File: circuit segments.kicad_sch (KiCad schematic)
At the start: 0 parts

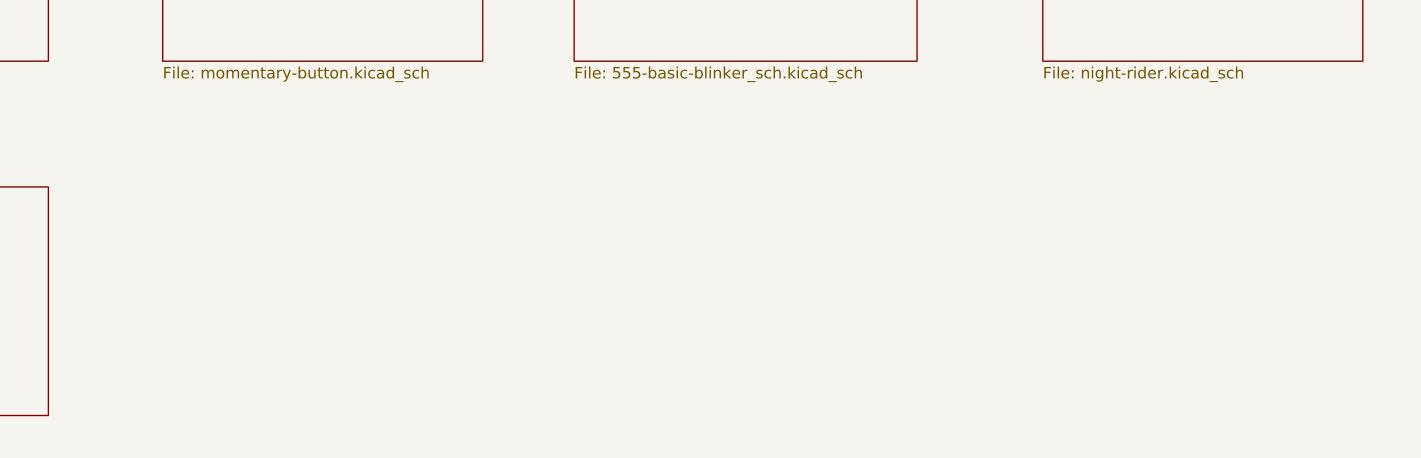
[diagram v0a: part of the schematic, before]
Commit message: new pages added
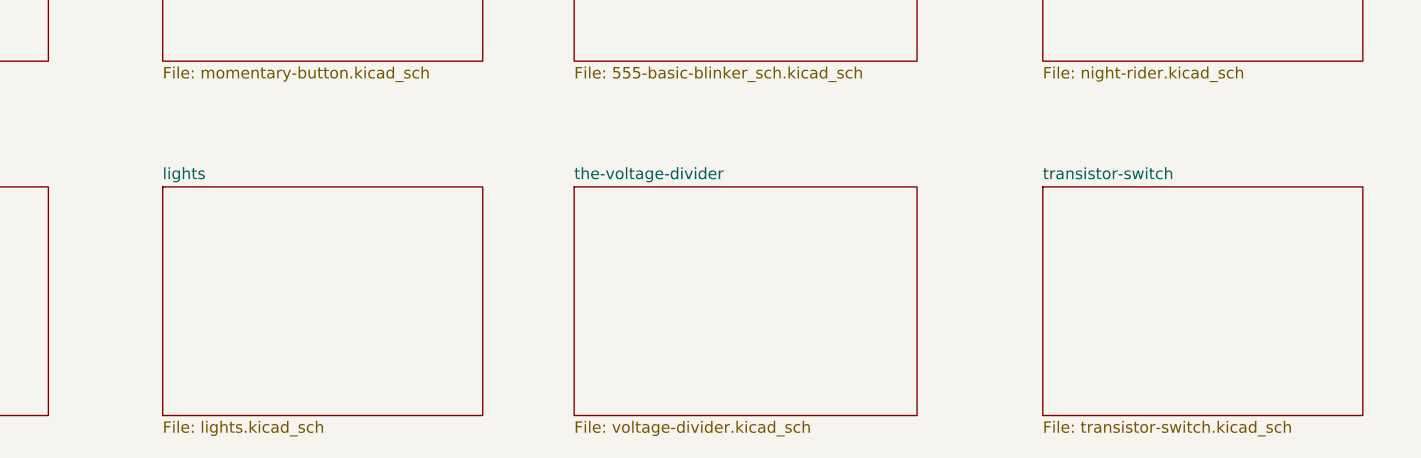
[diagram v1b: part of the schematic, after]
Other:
- added sheet lights (lights.kicad_sch)
- added sheet the-voltage-divider (voltage-divider.kicad_sch)
- added sheet transistor-switch (transistor-switch.kicad_sch)
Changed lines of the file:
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@@
+	)
+	(sheet
+		(at 184.15 92.71)
+		(size 35.56 25.4)
+		(fields_autoplaced yes)
+		(stroke
+			(width 0.1524)
+			(type solid)
+		)
+		(fill
+			(color 0 0 0 0.0000)
+		)
+		(property "Sheetname" "transistor-switch"
+			(at 184.15 91.9984 0)
+			(effects
+				(font
+					(size 1.27 1.27)
+				)
+				(justify left bottom)
+			)
+		)
+		(property "Sheetfile" "transistor-switch.kicad_sch"
+			(at 184.15 118.6946 0)
+			(effects
+				(font
+					(size 1.27 1.27)
+				)
+				(justify left top)
+			)
+		)
+		(instances
+			(project "circuit segments"
+				(path "/6128aede-be38-412f-a65d-6dbf7377b853"
+					(page "9")
+				)
+			)
+		)
 	)
 	(sheet
@@
 				)
 			)
+		)
+	)
+	(sheet
+		(at 86.36 92.71)
+		(size 35.56 25.4)
+		(fields_autoplaced yes)
+		(stroke
+			(width 0.1524)
+			(type solid)
+		)
+		(fill
+			(color 0 0 0 0.0000)
+		)
+		(property "Sheetname" "lights"
+			(at 86.36 91.9984 0)
+			(effects
+				(font
+					(size 1.27 1.27)
+				)
+				(justify left bottom)
+			)
+		)
+		(property "Sheetfile" "lights.kicad_sch"
+			(at 86.36 118.6946 0)
+			(effects
+				(font
+					(size 1.27 1.27)
+				)
+				(justify left top)
+			)
+		)
+		(instances
+			(project "circuit segments"
+				(path "/6128aede-be38-412f-a65d-6dbf7377b853"
+					(page "7")
+				)
+			)
+		)
+	)
+	(sheet
+		(at 132.08 92.71)
+		(size 38.1 25.4)
+		(fields_autoplaced yes)
+		(stroke
+			(width 0.1524)
+			(type solid)
+		)
+		(fill
+			(color 0 0 0 0.0000)
+		)
+		(property "Sheetname" "the-voltage-divider"
+			(at 132.08 91.9984 0)
+			(effects
+				(font
+					(size 1.27 1.27)
+				)
+				(justify left bottom)
+			)
+		)
+		(property "Sheetfile" "voltage-divider.kicad_sch"
+			(at 132.08 118.6946 0)
+			(effects
+				(font
+					(size 1.27 1.27)
+				)
+				(justify left top)
+			)
+		)
+		(property "Field2" ""
+			(at 132.08 92.71 0)
+			(effects
+				(font
+					(size 1.27 1.27)
+				)
+				(hide yes)
+			)
+		)
+		(instances
+			(project "circuit segments"
+				(path "/6128aede-be38-412f-a65d-6dbf7377b853"
+					(page "8")
+				)
+			)
